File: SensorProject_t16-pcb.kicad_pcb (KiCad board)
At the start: 2 copper layers, 48.3 x 71.1 mm, 90 parts, among them J1 Conn_01x02_Pin, J10 Conn_01x02_Pin, J11 Conn_01x02_Pin, J12 Conn_01x02_Pin, J13 Conn_01x02_Pin, J14 Conn_01x02_Pin, J15 Conn_01x02_Pin, J16 Conn_01x02_Pin, J17 Conn_01x04_Socket, J18 THTPad, J2 Conn_01x02_Pin, J20 Screw_Terminal_01x02, J21 Conn_2x02_Pin, J3 Conn_01x02_Pin, J4 Conn_01x02_Pin, J5 Conn_01x02_Pin, J6 Conn_01x02_Pin, J7 Conn_01x02_Pin, J8 Conn_01x02_Pin, J9 Conn_01x02_Pin, SW1 SW_Push, SW2 SW_Push, U1 ADS1115IDGS, U2 ADS1115IDGS, U3 ADS1115IDGS, U4 ADS1115IDGS, U5 STM32F411CEUx, U6 AMS1117-3.3, U7 RFM95W-915S2, Y1 25MHz, Y2 32.758kHz

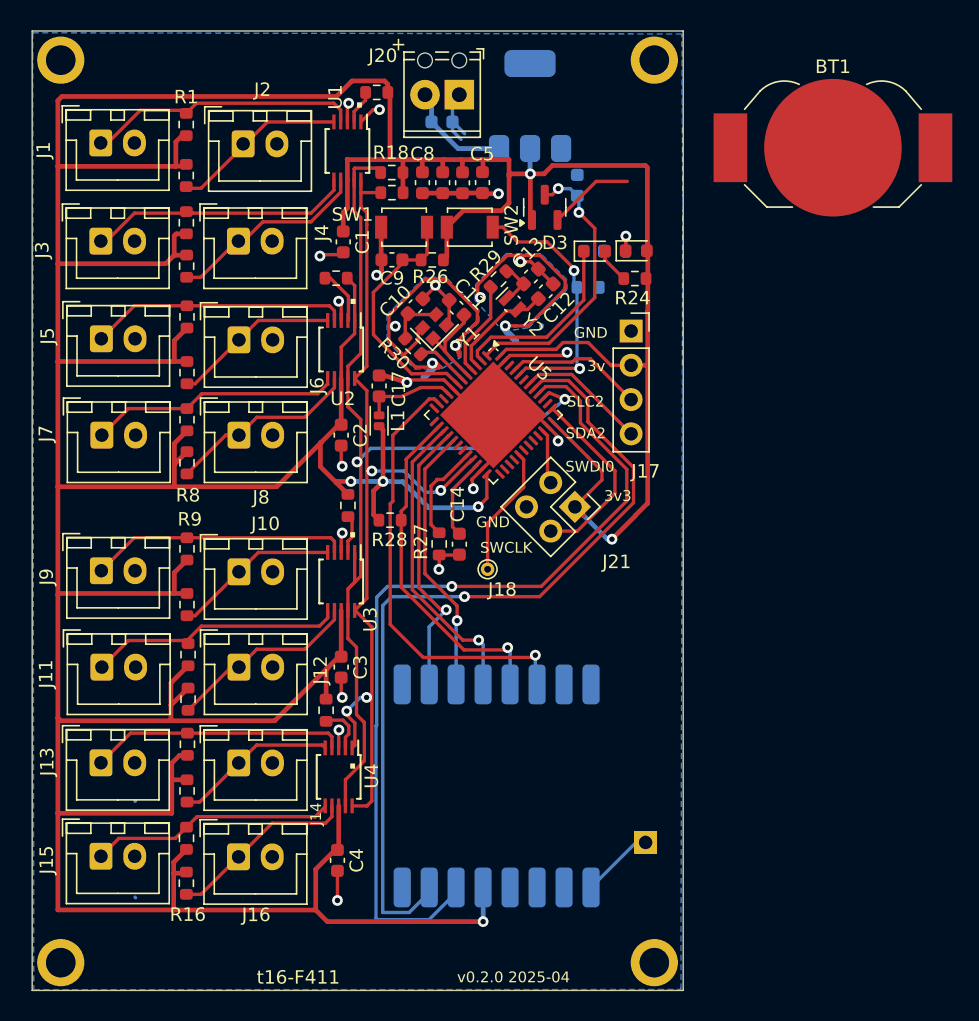
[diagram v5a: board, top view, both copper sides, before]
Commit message: battery in place. Need HSE xtal spec.
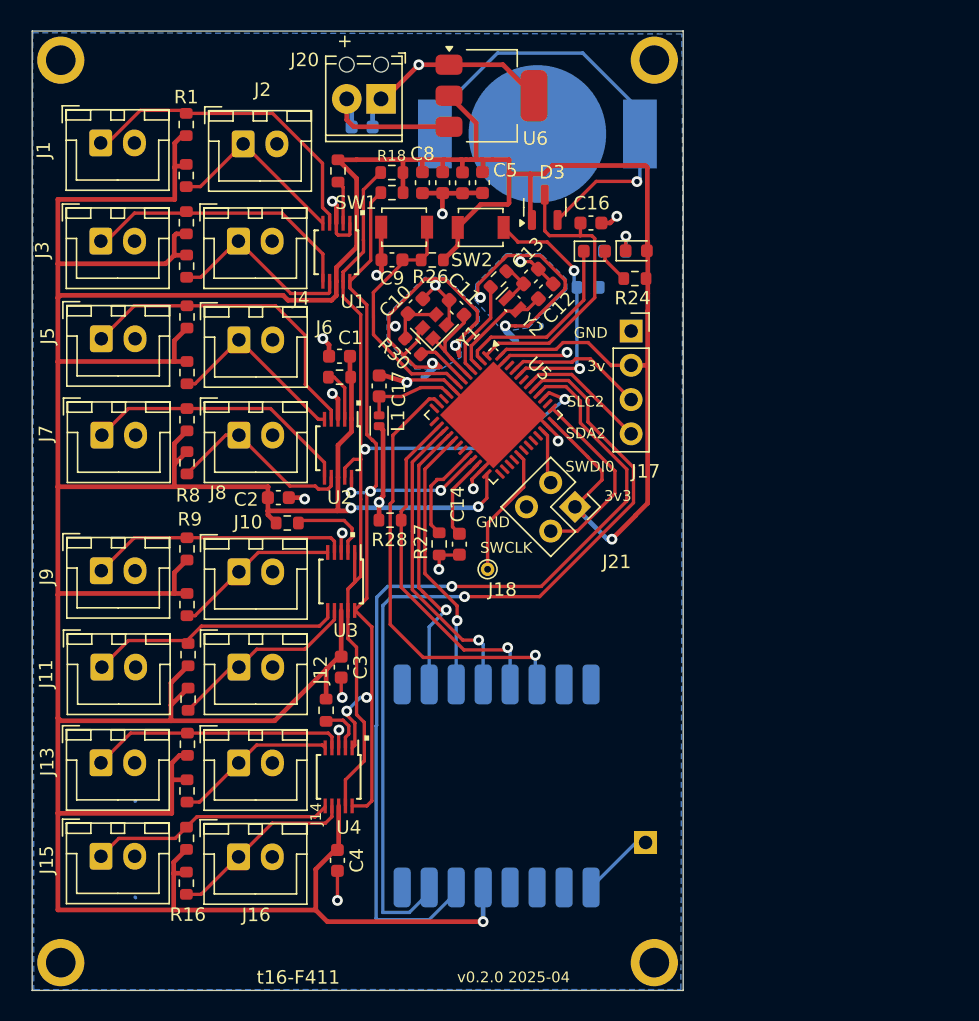
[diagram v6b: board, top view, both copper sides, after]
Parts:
- BT1: moved to B.Cu
- C16, U6: moved to F.Cu
- moved BT1 21.9 mm to (87.0, 31.8)
- moved C1 8.48 mm to (72.3, 48.2), turned to 180 degrees
- moved U1 7.55 mm to (72.1, 40.5)
- moved R20 7.34 mm to (72.3, 49.8)
- moved U2 7.33 mm to (72.2, 55.1)
- moved C2 6.57 mm to (67.8, 58.7), turned to 0 degrees
- moved R19 6.49 mm to (72.2, 34.5), turned to -90 degrees
- moved C15 5.93 mm to (74.0, 31.2)
- moved J20 5.81 mm to (75.4, 29.2)
- moved R21 4.68 mm to (68.4, 60.6), turned to 0 degrees
- moved C16 2.97 mm to (91.0, 38.4), turned to 0 degrees
- moved U6 2.96 mm to (83.6, 28.9), turned to 0 degrees
- moved SW2 0.81 mm to (82.8, 38.7)
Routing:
- net Net-(BT1-+): track 6.35 -> 32.7 mm, vias 0 -> 1
- net GND: track 66.7 -> 81.3 mm, vias 16 -> 17
- net +3V3: track 411.6 -> 402.9 mm, vias 6 -> 5
- net Net-(J5-Pin_1): track 19.2 -> 24.1 mm
- net +5V: track 8.04 -> 11.6 mm
- net Net-(J1-Pin_1): track 19.5 -> 22.9 mm
- net Net-(U3-ALERT/RDY): track 2.91 -> 6.15 mm
- net Net-(J7-Pin_1): track 18.3 -> 20.1 mm
- net Net-(J6-Pin_1): track 12.4 -> 14.0 mm
- net Net-(J2-Pin_1): track 12.5 -> 13.9 mm
- net VBAT: track 20.8 -> 21.8 mm, vias 2 -> 0
- net Net-(J3-Pin_1): track 19.0 -> 20.0 mm
- net SCL1: track 65.5 -> 66.4 mm, vias 4 -> 5
- net Net-(U5-BOOT0): track 19.8 -> 19.0 mm
- net Net-(U1-ALERT/RDY): track 2.54 -> 3.21 mm
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
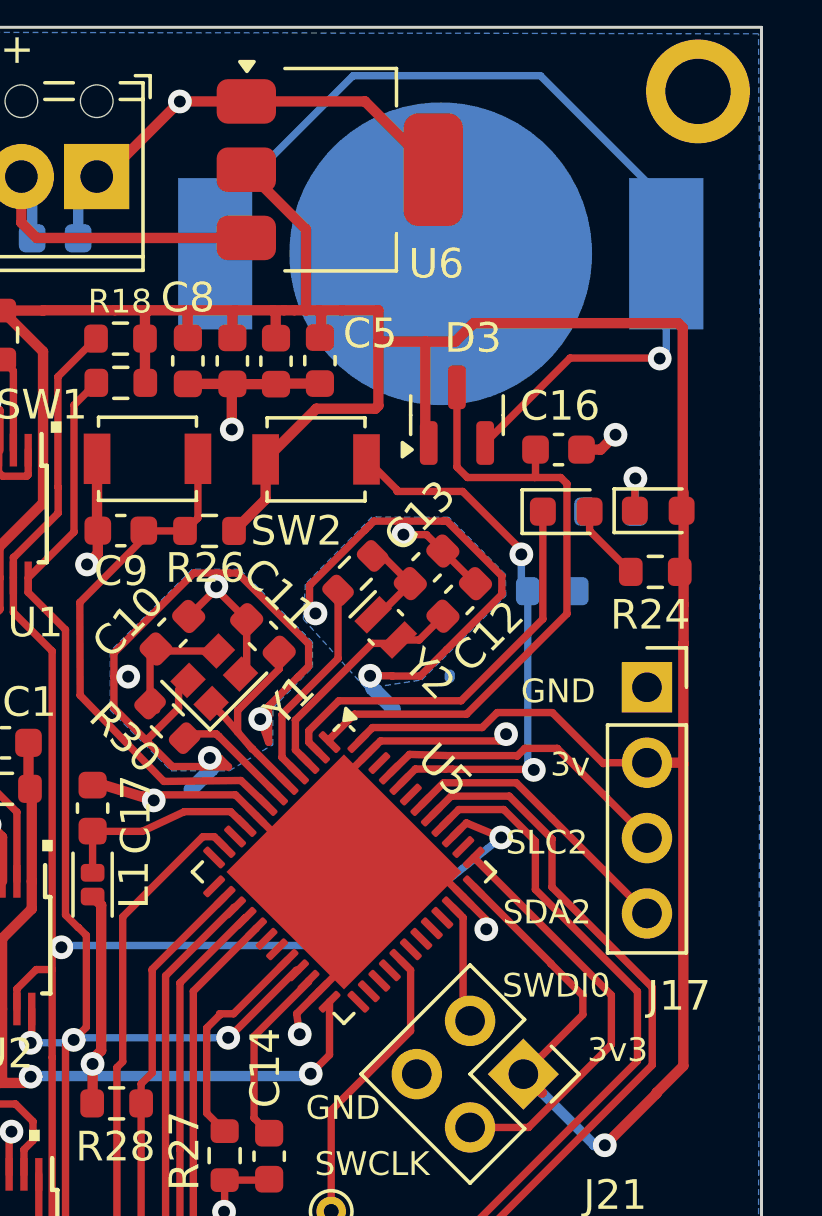
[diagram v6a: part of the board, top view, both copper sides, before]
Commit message: near complete, DRC good, ERC has a spurious error about ground on Y1.
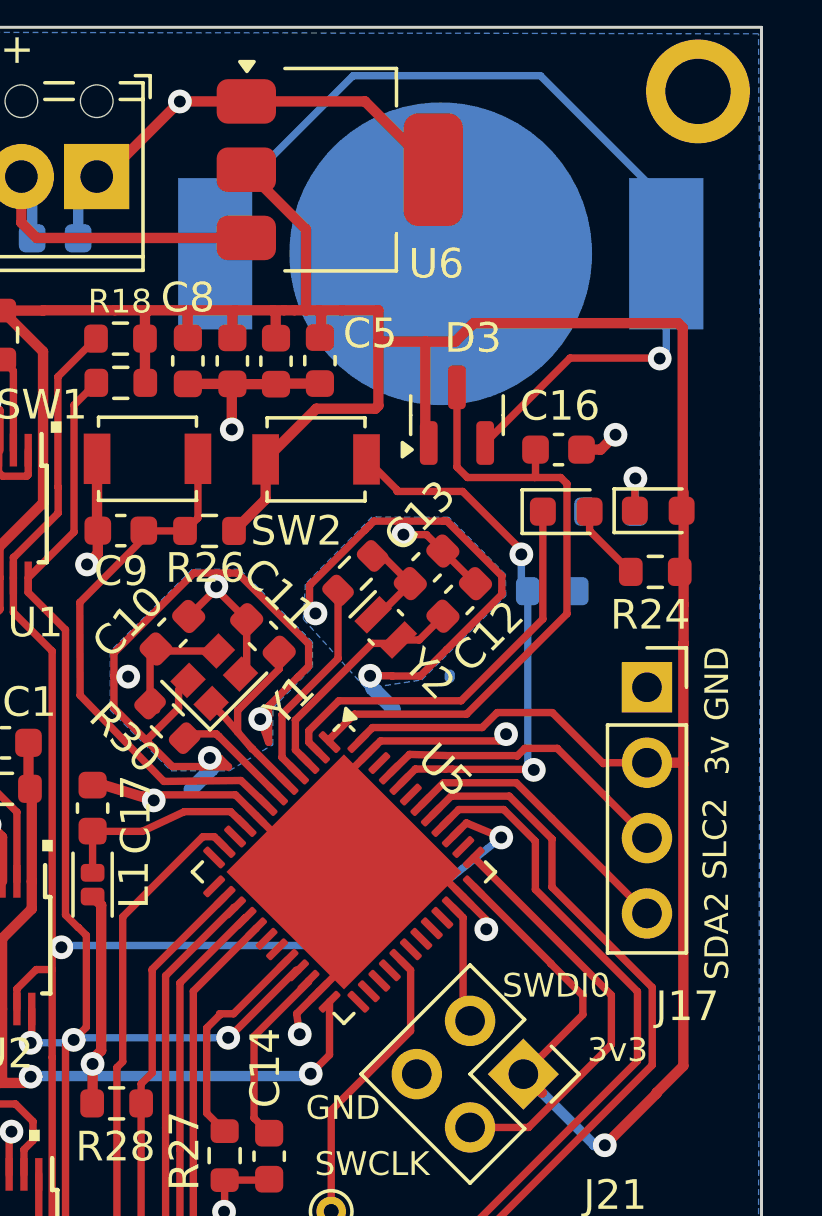
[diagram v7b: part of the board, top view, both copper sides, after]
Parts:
- BT1: value Battery_Cell -> Battery_Cell_Holder
- C10, C11: value 6pF C0G, NP0, +/- 0.1pF -> 10pF C0G, NP0, +/- 0.1pF
- R29: value CHECK K 1% -> 0
- R30: value 1.1k 1% -> 634 1%
- turned BT1 to 0 degrees

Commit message: cleanup, ready to submit.
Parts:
- C14: value 4.7uF -> 4.7µF
- C17: value 100n -> 100nF
- R23: value 0K4 -> 400
- R24: value 0K1 -> 100
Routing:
- net GND: track 81.3 -> 65.1 mm
- net Net-(BT1-+): track 32.7 -> 29.6 mm
- net +3V3: track 402.9 -> 401.2 mm
- net Net-(AE1-A): track 5.42 -> 4.71 mm
- net GND_HSE: track 30.1 -> 29.4 mm
- net SCL1: track 66.4 -> 65.7 mm
- net RESET: track 33.2 -> 32.7 mm
- net Net-(C10-Pad2): track 4.15 -> 3.63 mm
- net +5V: track 11.6 -> 11.1 mm
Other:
- board text added: "v0.2.0 2025-05"
- board text removed: "v0.2.0 2025-04"
